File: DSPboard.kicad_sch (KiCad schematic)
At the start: 0 parts

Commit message: add some components
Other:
- added sheet Power (Power.kicad_sch)
- added sheet uC&Codec (Main.kicad_sch)
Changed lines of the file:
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@@
 	(generator_version "9.0")
 	(paper "A4")
+	(sheet
+		(at 29.21 69.85)
+		(size 53.34 22.86)
+		(exclude_from_sim no)
+		(in_bom yes)
+		(on_board yes)
+		(dnp no)
+		(fields_autoplaced yes)
+		(stroke
+			(width 0.1524)
+			(type solid)
+		)
+		(fill
+			(color 0 0 0 0.0000)
+		)
+		(property "Sheetname" "Power"
+			(at 29.21 69.1384 0)
+			(effects
+				(font
+					(size 1.27 1.27)
+				)
+				(justify left bottom)
+			)
+		)
+		(property "Sheetfile" "Power.kicad_sch"
+			(at 29.21 93.2946 0)
+			(effects
+				(font
+					(size 1.27 1.27)
+				)
+				(justify left top)
+			)
+		)
+		(instances
+			(project "DSPboard"
+				(path "/ee8026cd-c8f1-4ab8-b3ed-795cda0e45f2"
+					(page "3")
+				)
+			)
+		)
+	)
+	(sheet
+		(at 29.21 29.21)
+		(size 74.93 27.94)
+		(exclude_from_sim no)
+		(in_bom yes)
+		(on_board yes)
+		(dnp no)
+		(fields_autoplaced yes)
+		(stroke
+			(width 0.1524)
+			(type solid)
+		)
+		(fill
+			(color 0 0 0 0.0000)
+		)
+		(property "Sheetname" "uC&Codec"
+			(at 29.21 28.4984 0)
+			(effects
+				(font
+					(size 1.27 1.27)
+				)
+				(justify left bottom)
+			)
+		)
+		(property "Sheetfile" "Main.kicad_sch"
+			(at 29.21 57.7346 0)
+			(effects
+				(font
+					(size 1.27 1.27)
+				)
+				(justify left top)
+			)
+		)
+		(instances
+			(project "DSPboard"
+				(path "/ee8026cd-c8f1-4ab8-b3ed-795cda0e45f2"
+					(page "2")
+				)
+			)
+		)
+	)
 	(sheet_instances
 		(path "/"

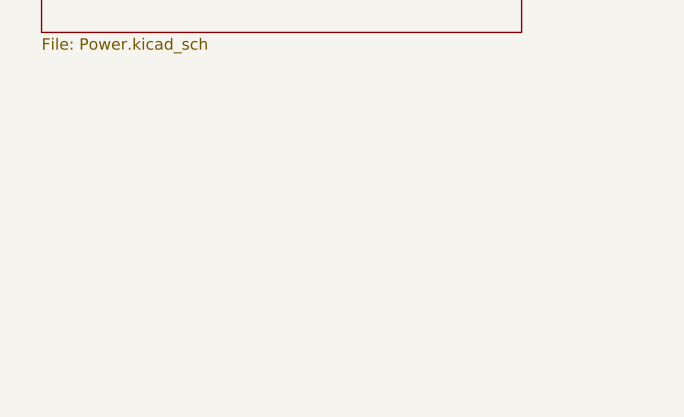
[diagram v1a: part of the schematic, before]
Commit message: add new sheet audio front
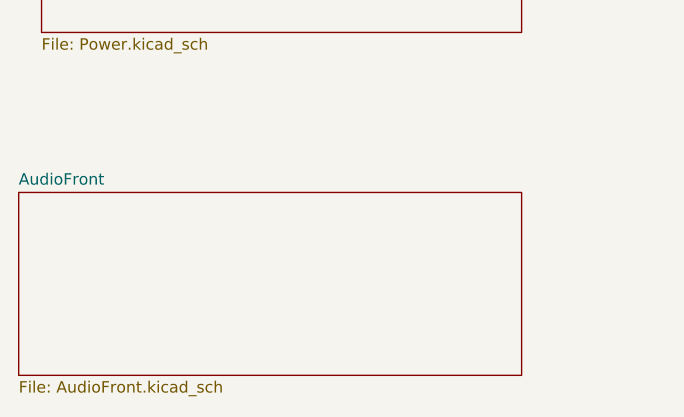
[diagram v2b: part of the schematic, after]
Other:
- added sheet AudioFront (AudioFront.kicad_sch)
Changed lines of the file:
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@@
+	)
+	(sheet
+		(at 26.67 110.49)
+		(size 55.88 20.32)
+		(exclude_from_sim no)
+		(in_bom yes)
+		(on_board yes)
+		(dnp no)
+		(fields_autoplaced yes)
+		(stroke
+			(width 0.1524)
+			(type solid)
+		)
+		(fill
+			(color 0 0 0 0.0000)
+		)
+		(property "Sheetname" "AudioFront"
+			(at 26.67 109.7784 0)
+			(effects
+				(font
+					(size 1.27 1.27)
+				)
+				(justify left bottom)
+			)
+		)
+		(property "Sheetfile" "AudioFront.kicad_sch"
+			(at 26.67 131.3946 0)
+			(effects
+				(font
+					(size 1.27 1.27)
+				)
+				(justify left top)
+			)
+		)
+		(instances
+			(project "DSPboard"
+				(path "/ee8026cd-c8f1-4ab8-b3ed-795cda0e45f2"
+					(page "4")
+				)
+			)
+		)
 	)
 	(sheet
